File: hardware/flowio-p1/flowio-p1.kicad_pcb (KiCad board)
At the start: 4 copper layers, 80 x 70 mm, 139 parts, among them J1 DC-005, J10 VALVE, J11 VALVE, J12 VALVE, J13 VALVE, J14 VALVE, J15 VALVE, J16 VALVE, J17 VALVE, J18 DEBUG-UART, J19 DEBUG-GPIO, J2 USB-C, J5 XH-4P, J6 XH-4P, J7 XH-4P, J8 XH-4P, J9 XH-4P, Q10 AO3400A, Q11 SS8050, Q12 SS8050, Q3 AO3400A, Q4 AO3400A, Q5 AO3400A, Q6 AO3400A, Q7 AO3400A, Q8 AO3400A, Q9 AO3400A, SW1 RST, SW2 BOOT, SW3 USER, U1 ESP32-S3-WROOM-1-N16R8, U2 TCA9548APWR, U3 TPS54331DR, U4 CH340K, U5 USBLC6-2SC6

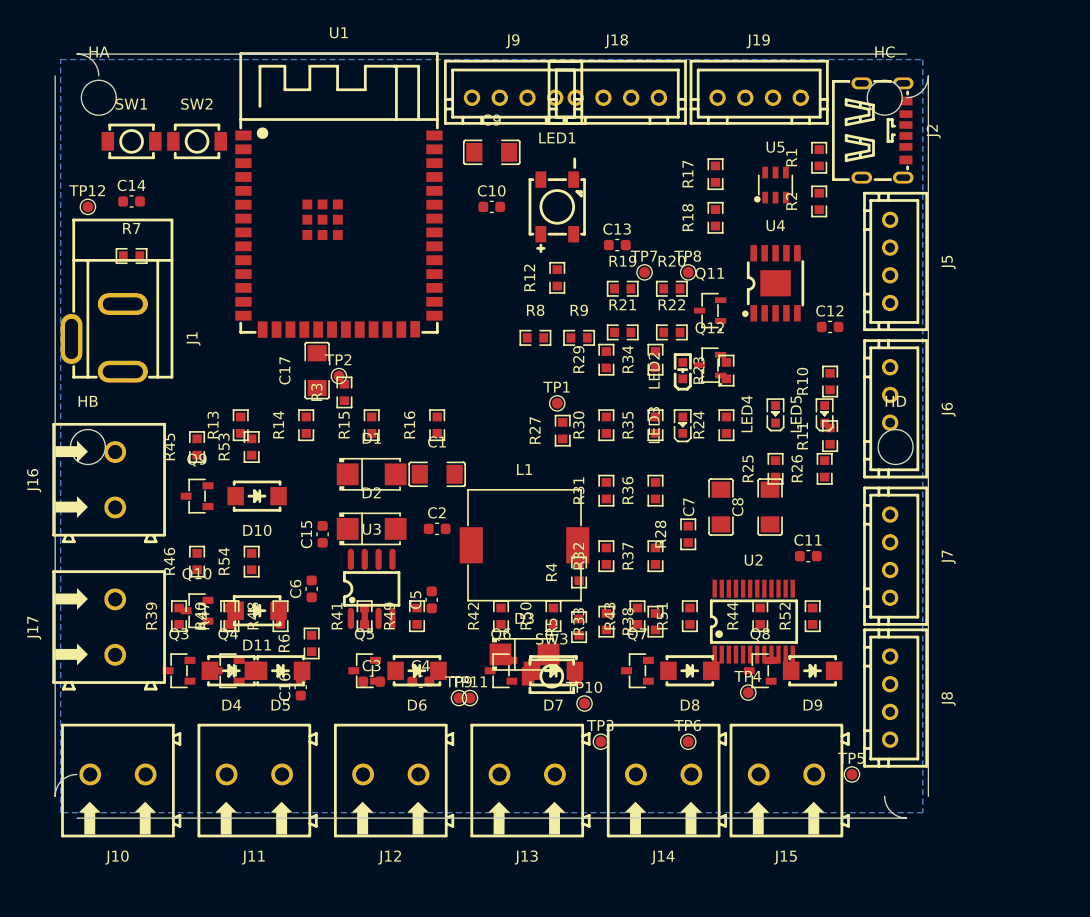
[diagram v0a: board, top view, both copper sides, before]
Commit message: feat: PCB 90×75 骨架定稿——布局收敛/层叠F信号+In1 GND+In2电源分区/电源过孔54/GND缝合36; 自动布线器(A*双层)已建但待完善, 剩余146未连接建议 Freerouting/GUI 完成
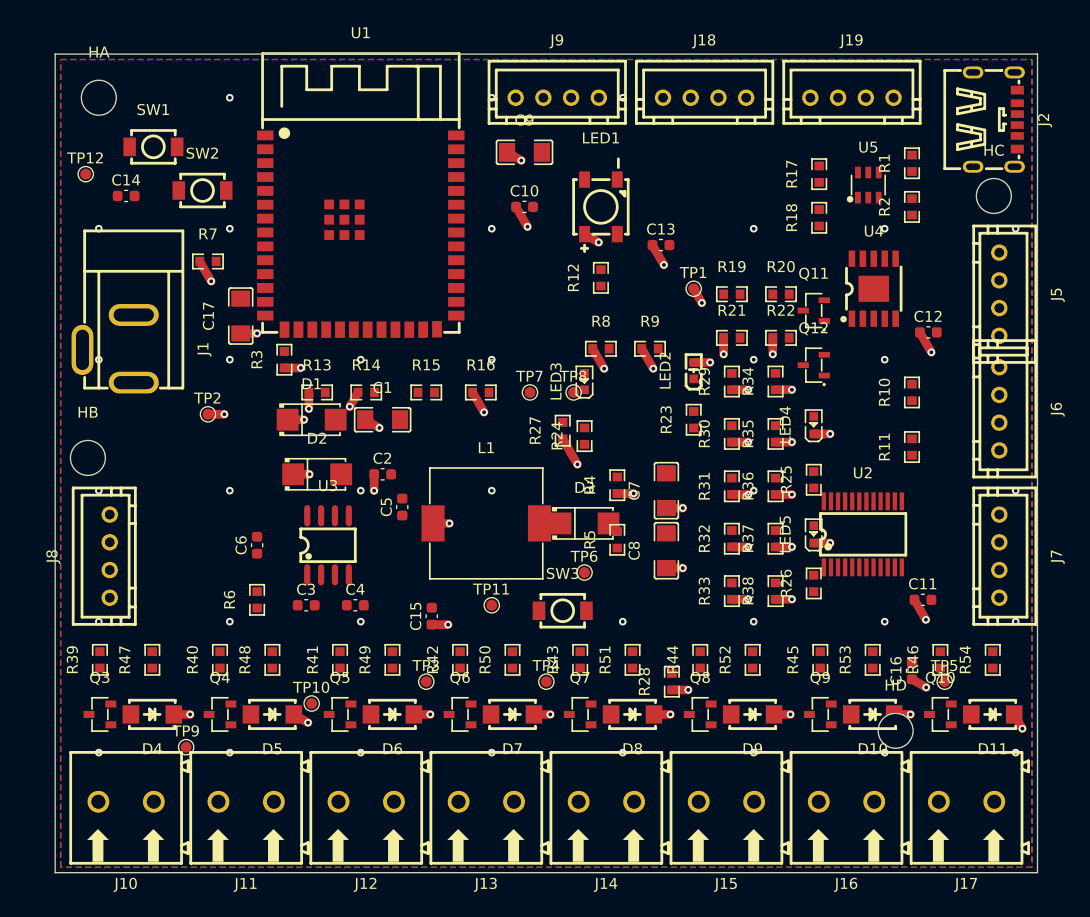
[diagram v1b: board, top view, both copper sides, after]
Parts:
- moved J17 79.6 mm to (83.5, 68.5), turned to 180 degrees
- moved J16 73.2 mm to (72.5, 68.5), turned to 180 degrees
- moved J8 72.7 mm to (5.00, 46.0), turned to 90 degrees
- moved Q10 68.8 mm to (81.1, 60.5)
- moved R46 68.7 mm to (81.1, 55.5)
- moved R54 68.5 mm to (85.9, 55.5)
- moved D11 68.1 mm to (85.9, 60.5)
- moved Q9 60.5 mm to (70.1, 60.5)
- moved R45 60.3 mm to (70.1, 55.5)
- moved R53 60.1 mm to (74.9, 55.5)
- moved D10 59.8 mm to (74.9, 60.5)
- moved C16 56.0 mm to (78.5, 56.5)
- moved HD 26.0 mm to (77.0, 62.0)
- moved TP9 25.4 mm to (12.0, 63.5)
- moved TP10 25.0 mm to (23.5, 59.5)
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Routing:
- net +3V3: track 0.00 -> 57.0 mm, vias 0 -> 35
- net +5V: track 0.00 -> 25.5 mm, vias 0 -> 17
- net GND: vias 0 -> 35
- added copper zone on F.Cu, net GND
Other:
- board size 80 x 70 mm -> 90 x 75 mm

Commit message: feat(P1): freerouting 双轮布线完成 146→17 未连接·零短路; 目视检查抓到并修复天线禁布区丢失
- baseline 采纳: freerouting v2.4.1 (headless CLI, DSN/SES 回灌) 两轮
  rip-up&reroute + BatchOptimizer; 佐证源码 MazeRipupResolver 的
  fanout 保护/ripup 代价机制 (FANOUT_COST_CONSTANT=20000)
- 布线后清理: 平面重建 (GND 全实连)、线宽 0.25→0.2 回退消除 130 间距
  违规、zones_intersect/starved_thermal 清零
- 目视检查 (用户强制要求) 顶/底 2400×2000 渲染逐区检查 + 程序化核实:
  * 发现 route_pcb.py 重建平面时删除了天线禁布区 → GND/+3V3 填充
    铺进 ESP32 天线正下方 (HitTestFilledArea 四层命中)
  * 修复: fix_keepout.py 补回 ANT_KEEPOUT rule area (x19.5-36.5/y0.2-6.4,
    四铜层禁填充/走线/过孔), 重灌后 6 探测点 0 命中, DRC 无新增
  * 安装孔 4 个全净空; 走线无交叉乱麻; 无出界铜
- 遗留: 17 未连接 (TCA GND/3V3 尾巴/J6.1/R14.1 等), 3 间距, 6 孔间距,
  2 悬空过孔; 外观类 52 silk_over_copper + 44 courtyard (JLC 可制)
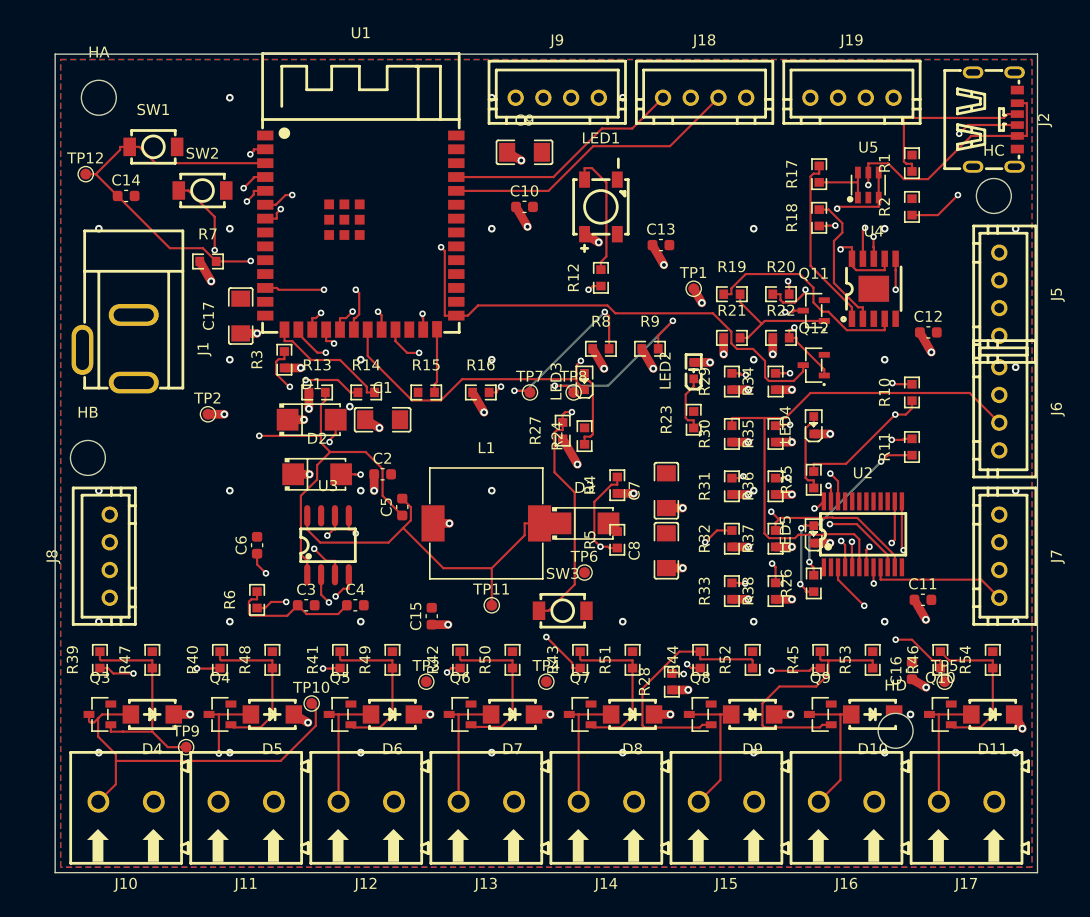
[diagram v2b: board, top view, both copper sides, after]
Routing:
- net BTN_USER: track 0.00 -> 151.0 mm, vias 0 -> 2
- net BOOT: track 0.00 -> 126.5 mm, vias 0 -> 3
- net EN: track 0.00 -> 89.0 mm, vias 0 -> 2
- net USB_VBUS: track 0.00 -> 86.6 mm, vias 0 -> 2
- net S4_SDA: track 0.00 -> 78.4 mm, vias 0 -> 2
- net I2C_SDA: track 0.00 -> 77.6 mm, vias 0 -> 4
- net S4_SCL: track 0.00 -> 76.1 mm, vias 0 -> 1
- net S5_SDA: track 0.00 -> 72.8 mm, vias 0 -> 2
- net LED_USER: track 0.00 -> 69.7 mm, vias 0 -> 1
- net S5_SCL: track 0.00 -> 68.8 mm, vias 0 -> 2
- net I2C_SCL: track 0.00 -> 68.4 mm, vias 0 -> 4
- net IO21: track 0.00 -> 67.0 mm, vias 0 -> 2
- net +3V3: track 57.0 -> 122.2 mm, vias 35 -> 39
- net UART_TX: track 0.00 -> 63.9 mm, vias 0 -> 1
- net UART_RX: track 0.00 -> 62.1 mm, vias 0 -> 1
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
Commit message: fix(pcb): 删坏+5V过孔+D10.1重连; HD(77,62)→(68,65)让出D10走廊 (hole 6→1, dangling 2→1)
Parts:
- moved HD 9.49 mm to (68.0, 65.0)
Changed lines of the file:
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@@
 	(footprint "MountingHole_3.2mm_M3"
 		(layer "F.Cu")
-		(at 77 62)
+		(at 68 65)
 		(descr "Mounting Hole 3.2mm, M3, no annular, generated by kicad-footprint-generator mountinghole.py")
 		(tags "mountinghole M3")
@@
 	)
 	(segment
+		(start 76.8649 60.5)
+		(end 77.165 60.5)
+		(width 0.4)
+		(layer "F.Cu")
+		(net "+5V")
+	)
+	(segment
 		(start 29.225 38.5)
 		(end 29.225 40)
@@
 	)
 	(via
+		(at 77.165 60.5)
+		(size 0.9)
+		(drill 0.45)
+		(layers "F.Cu" "B.Cu")
+		(net "+5V")
+	)
+	(via
 		(at 88.6149 61.799)
 		(size 0.7)
@@
 		(size 0.7)
 		(drill 0.35)
-		(layers "F.Cu" "B.Cu")
-		(net "+5V")
-	)
-	(via
-		(at 78.3649 60.5)
-		(size 0.7)
-		(drill 0.35)
